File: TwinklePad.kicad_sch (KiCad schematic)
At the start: 0 parts

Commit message: Made a complete schematic (maybe)
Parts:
- added A1: RaspberryPi_Pico_W, Module:RaspberryPi_Pico_W_SMD_HandSolder, symbol MCU_Module:RaspberryPi_Pico_W
- added D1, D10, D11, D12, D13, D14, D15, D16, D2, D3, D4, D5, D6, D7, D8, D9: SK6812MINI-E, HackPad:SK6812MINI-E_fixed, symbol SK6812MINI-E:SK6812MINI-E
- added D17, D18, D19, D20, D21, D22, D23, D24, D25, D26, D27, D28, D29, D30, D31, D32, D33, D34: D, Diode_THT:D_DO-35_SOD27_P7.62mm_Horizontal, symbol Device:D
- added J1: Conn_01x04_Pin, Connector_PinHeader_1.27mm:PinHeader_1x04_P1.27mm_Vertical, symbol Connector:Conn_01x04_Pin
- added REC_A1, REC_B1: RotaryEncoder_Switch, HackPad:RotaryEncoder_Alps_EC11E-Switch_Vertical_H20mm, symbol Device:RotaryEncoder_Switch
- added SW1, SW10, SW11, SW12, SW13, SW14, SW15, SW16, SW2, SW3, SW4, SW5, SW6, SW7, SW8, SW9: SW_Push, Button_Switch_Keyboard:SW_Cherry_MX_1.00u_PCB, symbol Switch:SW_Push
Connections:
- new net: D27.2 (A), SW11.2
- new net: D26.2 (A), SW10.2
- new net: D3.2 (DOUT), D7.4 (DIN)
- new net: D14.2 (DOUT), D3.4 (DIN)
- new net: D25.2 (A), SW9.2
- new net: D29.2 (A), SW13.2
- new net: D30.2 (A), SW14.2
- new net: D12.2 (DOUT), D16.4 (DIN)
- new net: D12.4 (DIN), D8.2 (DOUT)
- new net: D21.2 (A), SW5.2
- new net: D2.2 (DOUT), D6.4 (DIN)
- new net: D13.2 (DOUT), D2.4 (DIN)
- new net: D11.2 (DOUT), D15.4 (DIN)
- new net: D11.4 (DIN), D7.2 (DOUT)
- new net: D24.2 (A), SW8.2
- new net: D28.2 (A), SW12.2
- new net: D22.2 (A), SW6.2
- new net: D32.2 (A), SW16.2
- new net: D13.4 (DIN), D9.2 (DOUT)
- new net: D5.2 (DOUT), D9.4 (DIN)
- new net: D23.2 (A), SW7.2
- new net: D15.2 (DOUT), D4.4 (DIN)
- new net: D10.2 (DOUT), D14.4 (DIN)
- new net: D10.4 (DIN), D6.2 (DOUT)
- new net: D31.2 (A), SW15.2
- new net: D4.2 (DOUT), D8.4 (DIN)
- new net: D1.2 (DOUT), D5.4 (DIN)
- new net: D18.2 (A), SW2.2
- new net: D19.2 (A), SW3.2
- new net: D17.2 (A), SW1.2
- new net: D20.2 (A), SW4.2
- new net COL 0: A1.1 (GPIO0), SW1.1, SW2.1, SW3.1, SW4.1
- new net COL 1: A1.2 (GPIO1), SW5.1, SW6.1, SW7.1, SW8.1
- new net COL 2: A1.4 (GPIO2), SW10.1, SW11.1, SW12.1, SW9.1
- new net COL 3: A1.5 (GPIO3), SW13.1, SW14.1, SW15.1, SW16.1
- new net COL 4: A1.6 (GPIO4), REC_A1.S2, REC_B1.S2
- new net GND: A1.13 (GND), A1.18 (GND), A1.23 (GND), A1.28 (GND), A1.3 (GND), A1.38 (GND), A1.8 (GND), D1.3 (VSS), D10.3 (VSS), D11.3 (VSS), D12.3 (VSS), D13.3 (VSS), D14.3 (VSS), D15.3 (VSS), D16.3 (VSS), D2.3 (VSS), D3.3 (VSS), D4.3 (VSS), D5.3 (VSS), D6.3 (VSS), D7.3 (VSS), D8.3 (VSS), D9.3 (VSS), J1.4 (Pin_4), REC_A1.C, REC_B1.C
- new net OLED_SCL: A1.20 (GPIO15), J1.2 (Pin_2)
- new net OLED_SDA: A1.19 (GPIO14), J1.1 (Pin_1)
- new net REC_A1: A1.12 (GPIO9), REC_A1.B
- new net REC_A2: A1.14 (GPIO10), REC_A1.A
- new net REC_B1: A1.15 (GPIO11), REC_B1.B
- new net REC_B2: A1.16 (GPIO12), REC_B1.A
- new net REC_SW_A: D33.2 (A)
- new net REC_SW_A2: REC_A1.S1
- new net REC_SW_B: D34.2 (A)
- new net REC_SW_B2: REC_B1.S1
- new net RGB_DATA: A1.17 (GPIO13), D1.4 (DIN)
- new net ROW 0: A1.7 (GPIO5)
- new net ROW 1: A1.9 (GPIO6)
- new net ROW 2: A1.10 (GPIO7)
- new net ROW 3: A1.11 (GPIO8)
- new net ROW0: D17.1 (K), D21.1 (K), D25.1 (K), D29.1 (K), D33.1 (K)
- new net ROW1: D18.1 (K), D22.1 (K), D26.1 (K), D30.1 (K), D34.1 (K)
- new net ROW2: D19.1 (K), D23.1 (K), D27.1 (K), D31.1 (K)
- new net ROW3: D20.1 (K), D24.1 (K), D28.1 (K), D32.1 (K)
- new net VCC: A1.40 (VBUS), D1.1 (VDD), D10.1 (VDD), D11.1 (VDD), D12.1 (VDD), D13.1 (VDD), D14.1 (VDD), D15.1 (VDD), D16.1 (VDD), D2.1 (VDD), D3.1 (VDD), D4.1 (VDD), D5.1 (VDD), D6.1 (VDD), D7.1 (VDD), D8.1 (VDD), D9.1 (VDD), J1.3 (Pin_3)
- no-connect marks 0 -> 17
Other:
- note added: "ENCODERS"
- note added: "OLED DISPLAY"
- note added: "PICO CONTROLLER"
- note added: "RGB MATRIX"
- note added: "SWITCH MATRIX"

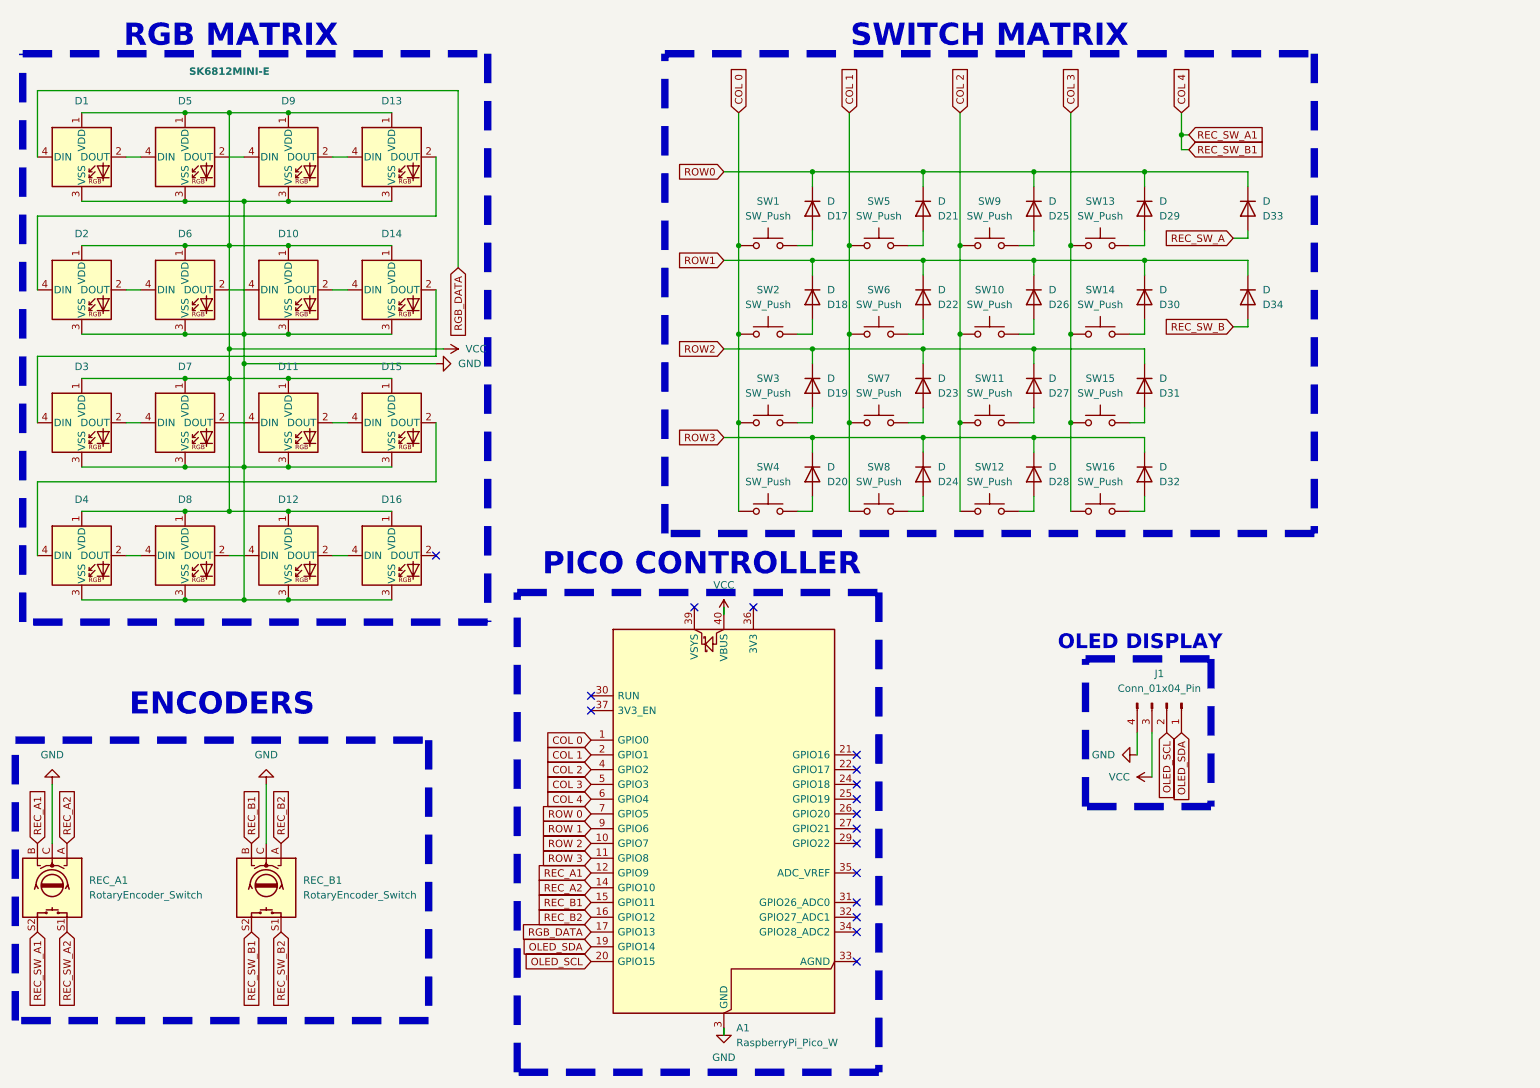
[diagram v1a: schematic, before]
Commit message: Currently moving keys to layout
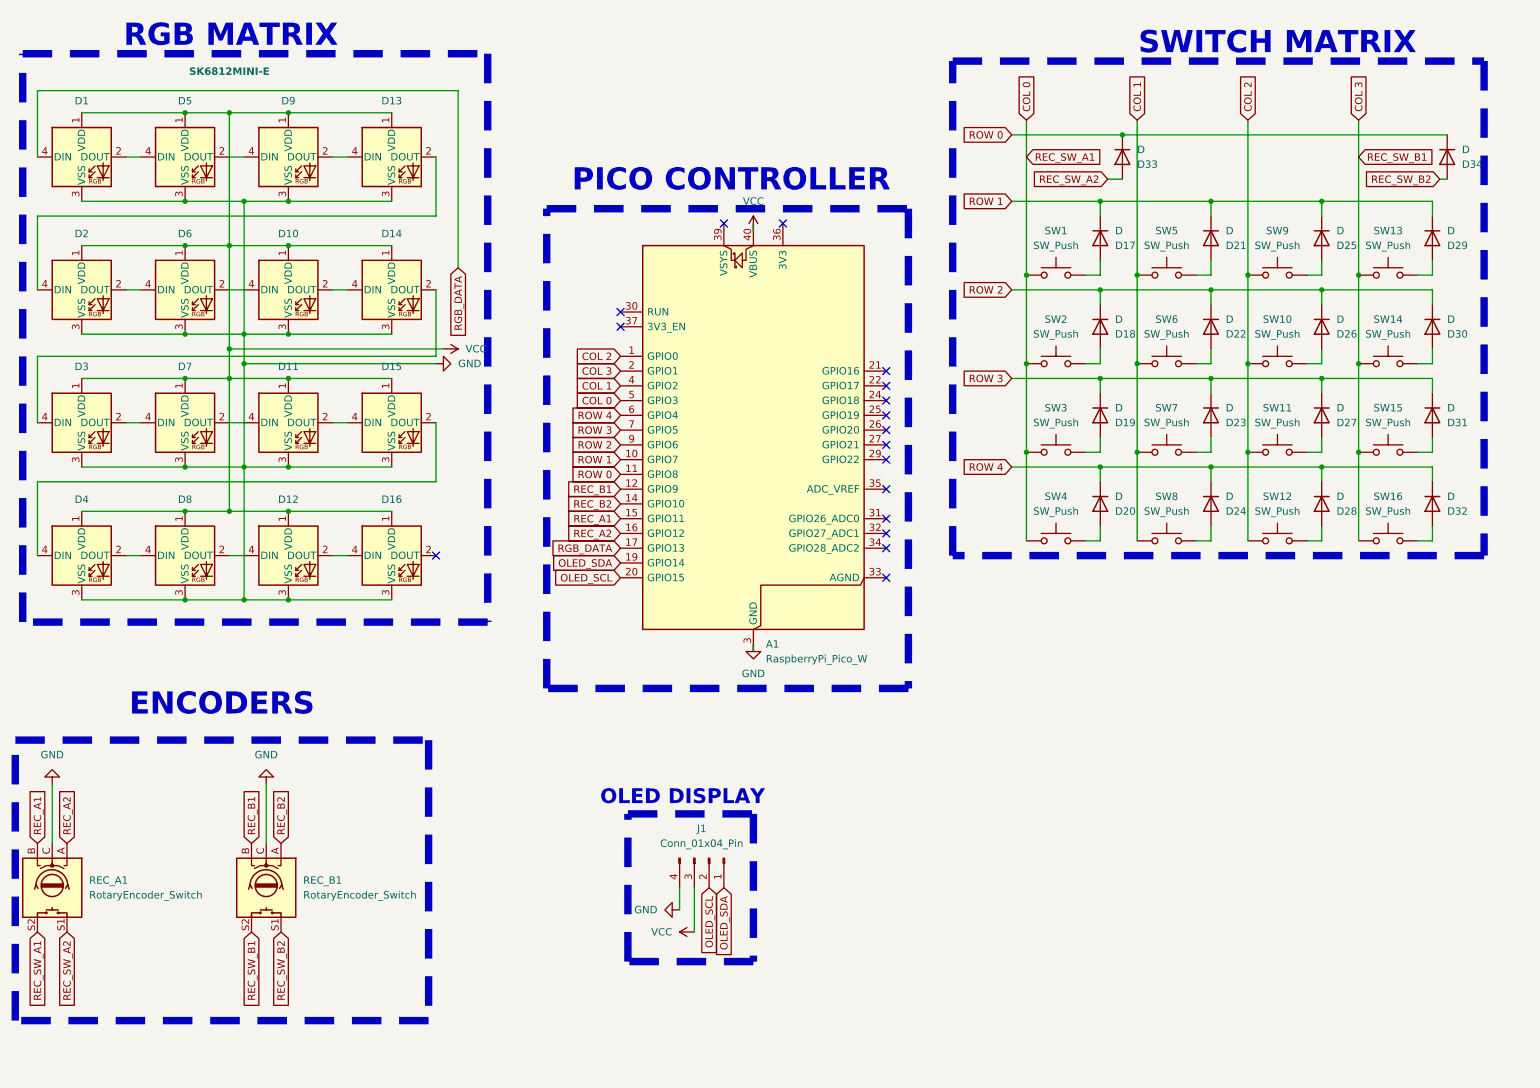
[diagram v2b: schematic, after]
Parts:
- A1: footprint Module:RaspberryPi_Pico_W_SMD_HandSolder -> Module:RaspberryPi_Pico_Common_Unspecified
- J1: footprint Connector_PinHeader_1.27mm:PinHeader_1x04_P1.27mm_Vertical -> Llama_Other:SSD1306-0.91-OLED-4pin-128x32
- SW1, SW10, SW11, SW12, SW13, SW14, SW15, SW16, SW2, SW3, SW4, SW5, SW6, SW7, SW8, SW9: footprint Button_Switch_Keyboard:SW_Cherry_MX_1.00u_PCB -> Switch_MX_Hotswap:MX-Hotswap-1U
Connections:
- net REC_SW_A is gone; now on net REC_SW_A2: D33.2 (A)
- net REC_SW_B is gone; now on net REC_SW_B2: D34.2 (A)
- net ROW2 is gone; now on net ROW 3: D19.1 (K), D23.1 (K), D27.1 (K), D31.1 (K)
- net COL 0: now also A1.5 (GPIO3), REC_A1.S2; no longer A1.1 (GPIO0)
- net COL 1: now also A1.4 (GPIO2); no longer A1.2 (GPIO1)
- net COL 2: now also A1.1 (GPIO0); no longer A1.4 (GPIO2)
- net COL 3: now also A1.2 (GPIO1), REC_B1.S2; no longer A1.5 (GPIO3)
- net REC_A1: now also A1.15 (GPIO11); no longer A1.12 (GPIO9)
- net REC_A2: now also A1.16 (GPIO12); no longer A1.14 (GPIO10)
- net REC_B1: now also A1.12 (GPIO9); no longer A1.15 (GPIO11)
- net REC_B2: now also A1.14 (GPIO10); no longer A1.16 (GPIO12)
- net ROW 0: now also A1.11 (GPIO8), D33.1 (K), D34.1 (K); no longer A1.7 (GPIO5)
- net ROW 1: now also A1.10 (GPIO7), D17.1 (K), D21.1 (K), D25.1 (K), D29.1 (K); no longer A1.9 (GPIO6)
- net ROW 2: now also A1.9 (GPIO6), D18.1 (K), D22.1 (K), D26.1 (K), D30.1 (K); no longer A1.10 (GPIO7)
- net ROW 3: now also A1.7 (GPIO5); no longer A1.11 (GPIO8)
- removed net COL 4: A1.6 (GPIO4), REC_A1.S2, REC_B1.S2
- removed net ROW0: D17.1 (K), D21.1 (K), D25.1 (K), D29.1 (K), D33.1 (K)
- removed net ROW1: D18.1 (K), D22.1 (K), D26.1 (K), D30.1 (K), D34.1 (K)
- net ROW3 renamed ROW 4
- net ROW 4: now also A1.6 (GPIO4)
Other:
- moved on the sheet: A1, D17, D18, D19, D20, D21, D22, D23, D24, D25, D26, D27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

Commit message: Finished PCB
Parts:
- added J2: Conn_01x02, Connector_PinHeader_2.54mm:PinHeader_1x02_P2.54mm_Vertical, symbol Connector_Generic:Conn_01x02
- added J3: AudioJack4, Connector_Audio:Jack_3.5mm_PJ320D_Horizontal, symbol Connector_Audio:AudioJack4
- added Q1: S8050, Package_TO_SOT_THT:TO-92_Inline, symbol Transistor_BJT:S8050
- added SW17: SW_DP3T, Connector_PinHeader_2.54mm:PinHeader_1x04_P2.54mm_Vertical, symbol Switch:SW_DP3T
- REC_A1, REC_B1: footprint HackPad:RotaryEncoder_Alps_EC11E-Switch_Vertical_H20mm -> RotaryEncoder:RotaryEncoder_Alps_EC11E-Switch_Vertical_H20mm
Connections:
- net COL 0: now also A1.7 (GPIO5); no longer A1.5 (GPIO3)
- net COL 1: now also A1.6 (GPIO4); no longer A1.4 (GPIO2)
- net COL 2: now also A1.5 (GPIO3); no longer A1.1 (GPIO0)
- net COL 3: now also A1.4 (GPIO2); no longer A1.2 (GPIO1)
- net GND: now also J3.S, Q1.1 (E)
- net OLED_SCL: now also A1.22 (GPIO17); no longer A1.20 (GPIO15)
- net OLED_SDA: now also A1.21 (GPIO16); no longer A1.19 (GPIO14)
- net REC_A1: now also A1.17 (GPIO13); no longer A1.15 (GPIO11)
- net REC_A2: now also A1.19 (GPIO14); no longer A1.16 (GPIO12)
- net REC_B1: now also A1.15 (GPIO11); no longer A1.12 (GPIO9)
- net REC_B2: now also A1.16 (GPIO12); no longer A1.14 (GPIO10)
- net RGB_DATA: now also A1.20 (GPIO15); no longer A1.17 (GPIO13)
- net ROW 0: now also A1.14 (GPIO10); no longer A1.11 (GPIO8)
- net ROW 1: now also A1.12 (GPIO9); no longer A1.10 (GPIO7)
- net ROW 2: now also A1.11 (GPIO8); no longer A1.9 (GPIO6)
- net ROW 3: now also A1.10 (GPIO7); no longer A1.7 (GPIO5)
- net ROW 4: now also A1.9 (GPIO6); no longer A1.6 (GPIO4)
- net VCC: now also J2.1 (Pin_1)
- net Buzzer+: now reaches A1.24 (GPIO18)
- net Buzzer+: now also Q1.2 (B)
- net Mode: now reaches A1.25 (GPIO19)
- net Mode: now also SW17.3
- net Mode 1: now reaches A1.26 (GPIO20)
- net Mode 1: now also SW17.1
- net Mode 2: now reaches A1.27 (GPIO21)
- net Mode 2: now also SW17.2
- net Mode 3: now reaches A1.29 (GPIO22)
- net Mode 3: now also SW17.4
- new net: J2.2 (Pin_2), Q1.3 (C)
- new net RX: A1.2 (GPIO1), J3.R1
- new net TX: A1.1 (GPIO0), J3.T
- no-connect marks 17 -> 11

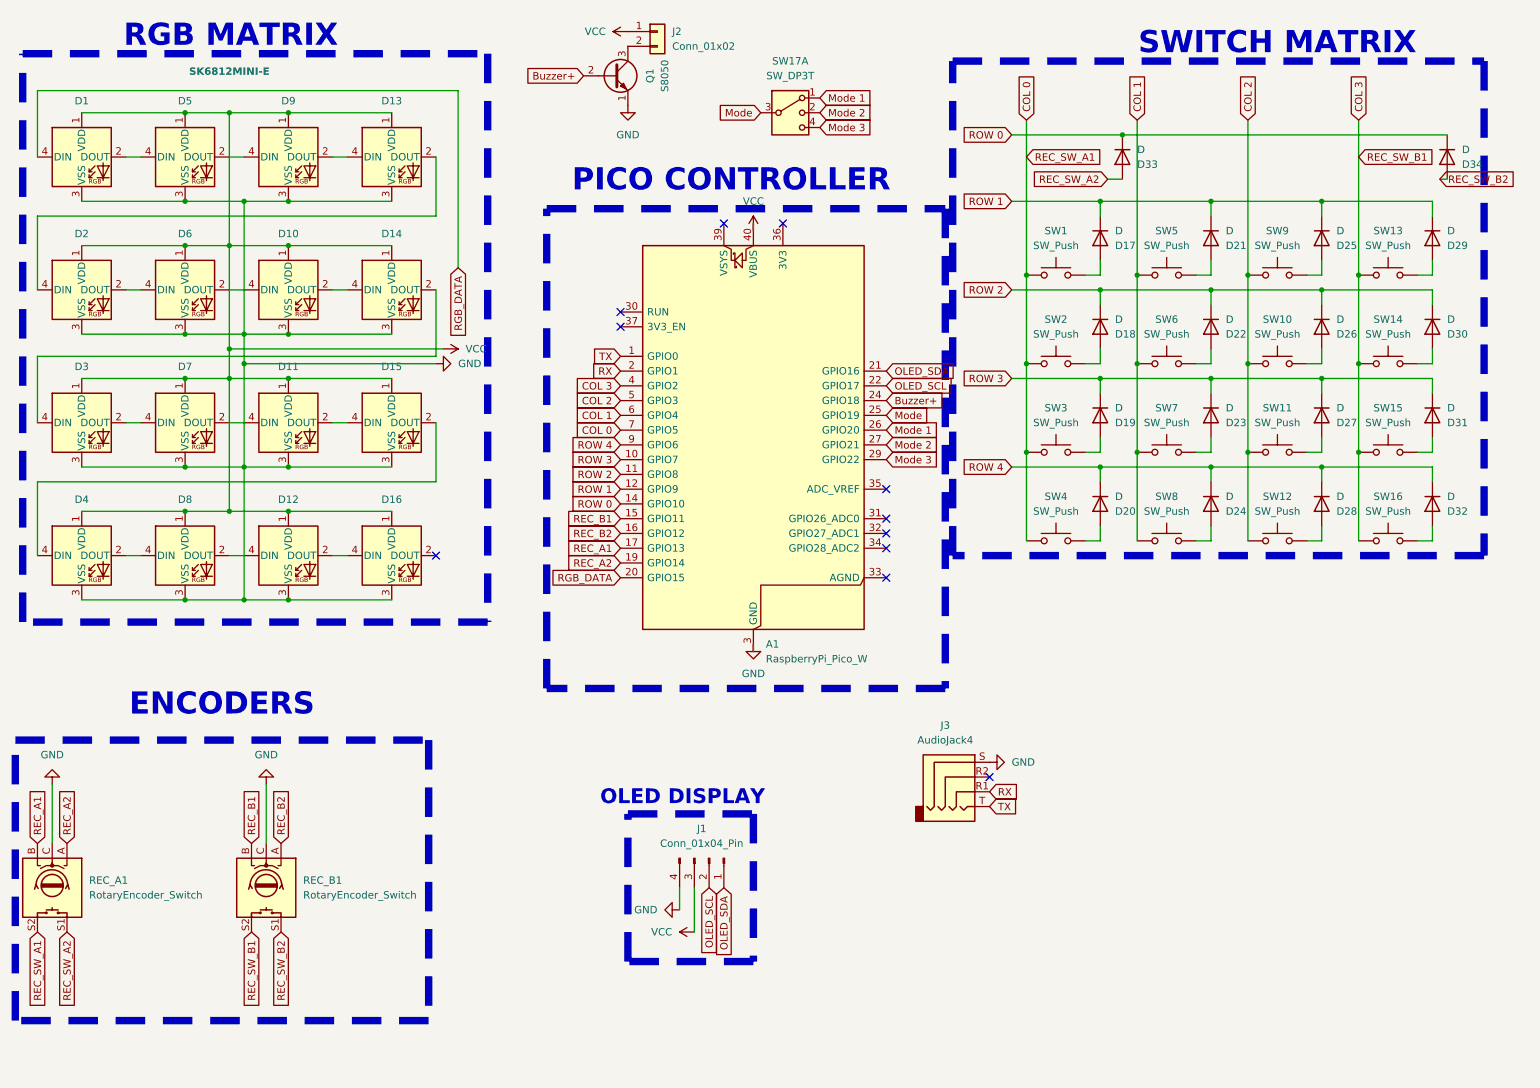
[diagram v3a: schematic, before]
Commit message: Updated PCB with new models and schematics
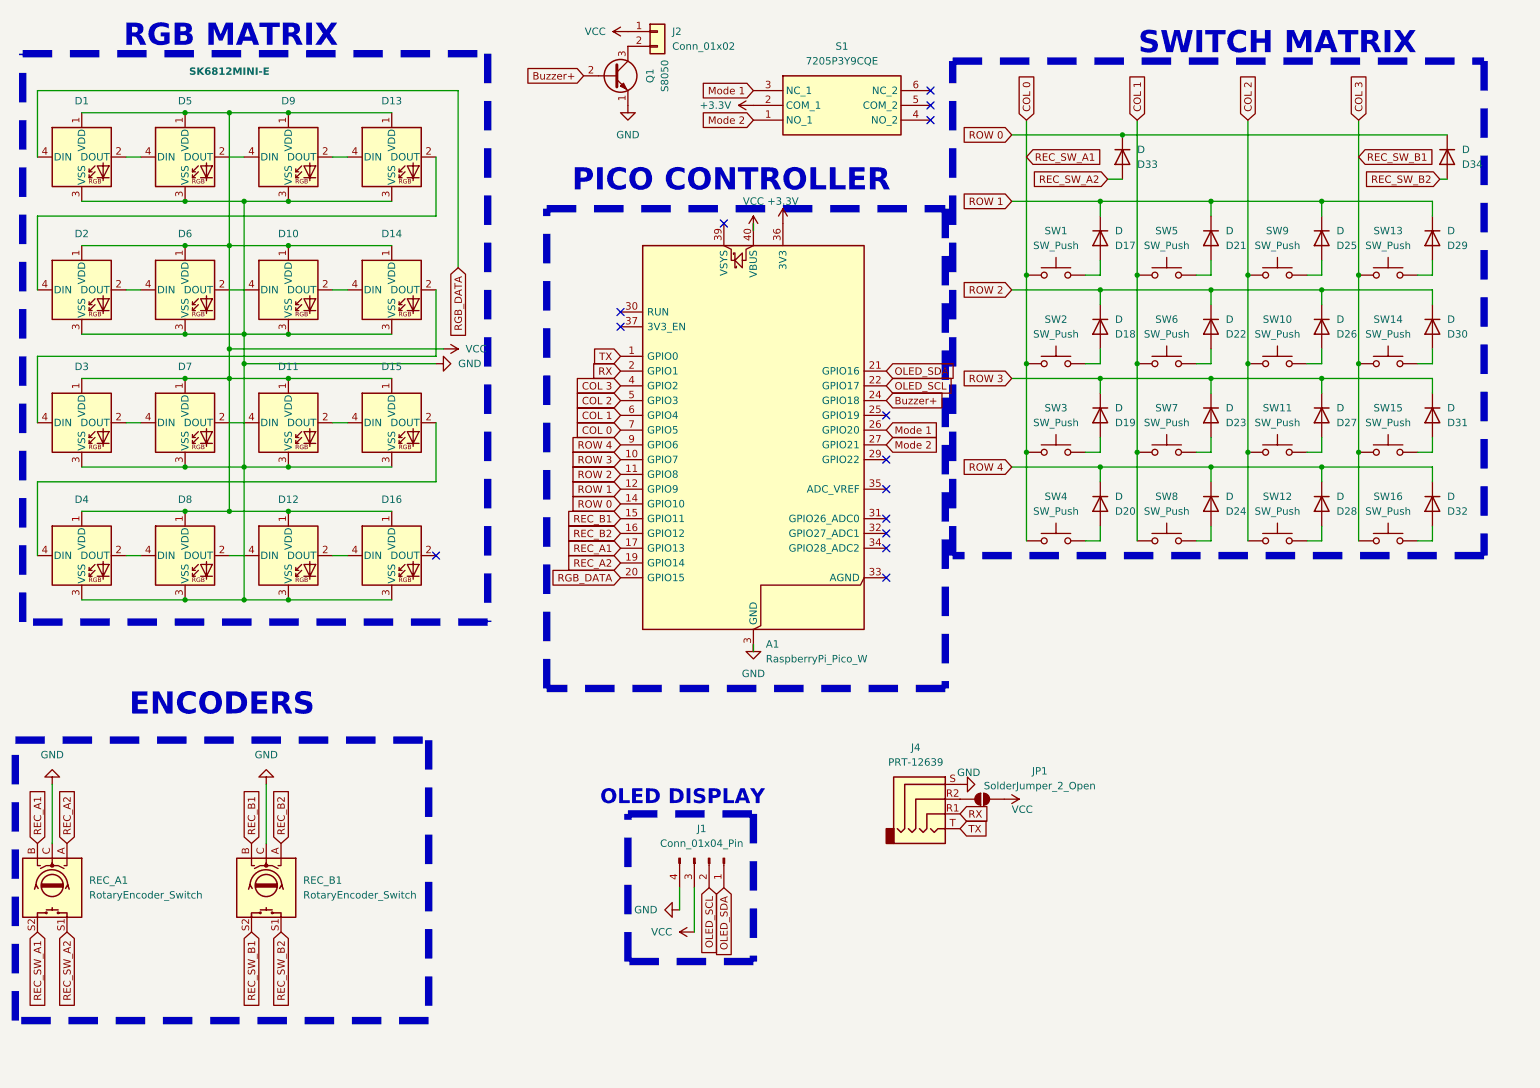
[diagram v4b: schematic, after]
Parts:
- removed J3: AudioJack4, Connector_Audio:Jack_3.5mm_PJ320D_Horizontal, symbol Connector_Audio:AudioJack4
- removed SW17: SW_DP3T, Connector_PinHeader_2.54mm:PinHeader_1x04_P2.54mm_Vertical, symbol Switch:SW_DP3T
- added J4: PRT-12639, PRT-12639:PRT12639, symbol Connector_Audio:AudioJack4
- added JP1: SolderJumper_2_Open, Jumper:SolderJumper-2_P1.3mm_Open_RoundedPad1.0x1.5mm, symbol Jumper:SolderJumper_2_Open
- added S1: 7205P3Y9CQE, Switch_DPDT_2x03:7205P3Y9CQE, symbol 7205P3Y9CQE:7205P3Y9CQE
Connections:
- net GND: now also J4.S
- net Mode 1: now also S1.3 (NC_1)
- net Mode 2: now also S1.1 (NO_1)
- net RX: now also J4.R1
- net TX: now also J4.T
- net VCC: now also JP1.2 (B)
- net +3.3V: now reaches A1.36 (3V3)
- net +3.3V: now also S1.2 (COM_1)
- net Mode: no longer names the net of A1.25 (GPIO19)
- net Mode 3: no longer names the net of A1.29 (GPIO22)
- new net: J4.R2, JP1.1 (A)
- no-connect marks 11 -> 14
